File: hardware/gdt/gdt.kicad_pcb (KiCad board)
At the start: 2 copper layers, 76.8 x 34.3 mm, 28 parts, among them J1 USB_OTG, J2 USB_A, Q1 Q_NPN_BEC, Q2 Q_NPN_BEC, Q3 Q_NMOS_GDS, U1 CH340G, U2 AP1117-33, U3 ESP-12E, Y1 12M

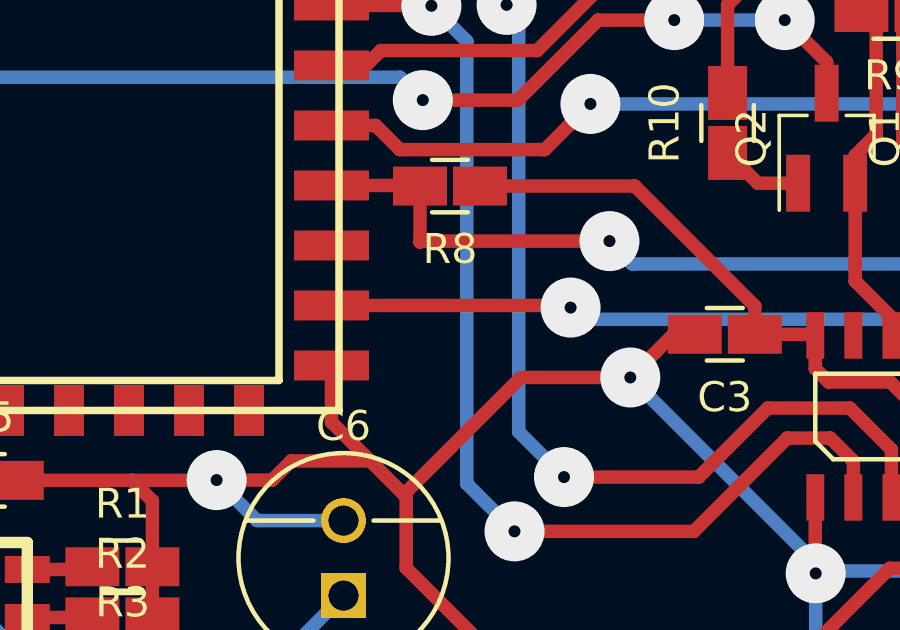
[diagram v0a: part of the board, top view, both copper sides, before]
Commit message: Whoops; this put it into boot mode 5 during reset rather than 1 -- forgot a pulldown resistor.
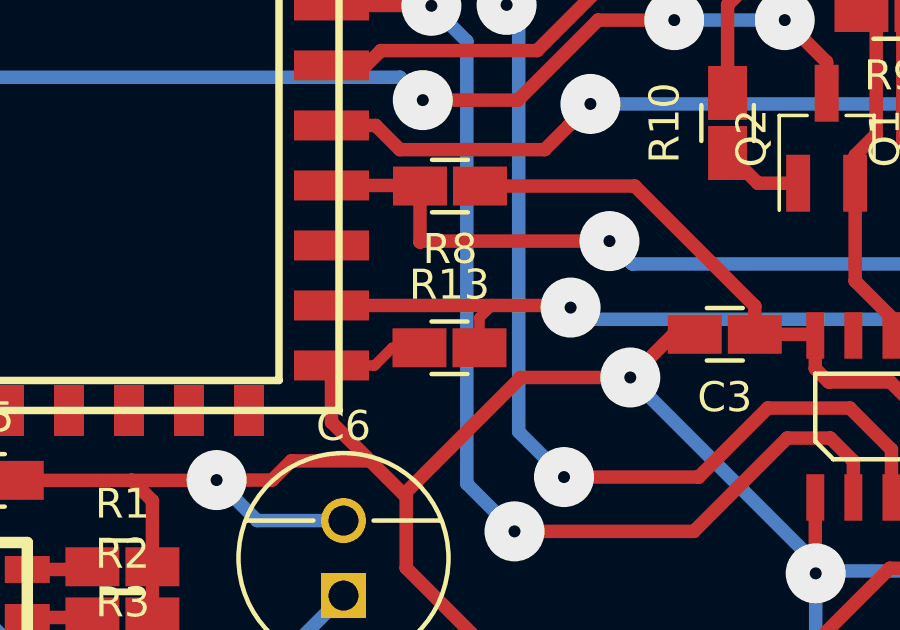
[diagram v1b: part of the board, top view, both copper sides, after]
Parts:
- added R13: 10k, coddingtonbear/coddingtonbear.pretty:0805_Milling, F.Cu at (121.4, 53.3)
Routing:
- net GND: track 186.7 -> 189.9 mm
- net Net-(Q3-Pad1): track 43.1 -> 44.7 mm
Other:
- net class Default: trace_width 0.45 -> 0.25
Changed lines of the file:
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@@
     (thickness 1.6)
     (drawings 4)
-    (tracks 349)
+    (tracks 355)
     (zones 0)
-    (modules 28)
+    (modules 29)
     (nets 42)
   )
@@
   )
   (setup
-    (last_trace_width 0.45)
+    (last_trace_width 0.35)
     (user_trace_width 0.35)
     (trace_clearance 0.2)
@@
   (net_class Default "This is the default net class."
     (clearance 0.2)
-    (trace_width 0.45)
+    (trace_width 0.25)
     (via_dia 2)
     (via_drill 0.4)
@@
     (add_net RXD)
     (add_net TXD)
+  )
+  (module coddingtonbear/coddingtonbear.pretty:0805_Milling (layer F.Cu)
+    (at 121.412 53.34)
+    (descr "Resistor SMD 0805, reflow soldering, Vishay (see dcrcw.pdf)")
+    (tags "resistor 0805")
+    (attr smd)
+    (fp_text reference R13 (at 0 -2.1) (layer F.SilkS)
+      (effects (font (size 1 1) (thickness 0.15)))
+    )
+    (fp_text value 10k (at 0 2.1) (layer F.Fab)
+      (effects (font (size 1 1) (thickness 0.15)))
+    )
+    (fp_line (start -0.6 -0.875) (end 0.6 -0.875) (layer F.SilkS) (width 0.15))
+    (fp_line (start 0.6 0.875) (end -0.6 0.875) (layer F.SilkS) (width 0.15))
+    (pad 2 smd rect (at 1 0) (size 1.8 1.3) (layers F.Cu F.Paste F.Mask)
+      (net 41 "Net-(Q3-Pad1)"))
+    (pad 1 smd rect (at -1 0) (size 1.8 1.3) (layers F.Cu F.Paste F.Mask)
+      (net 2 GND))
+    (model Resistors_SMD.3dshapes/R_0805.wrl
+      (at (xyz 0 0 0))
+      (scale (xyz 1 1 1))
+      (rotate (xyz 0 0 0))
+    )
   )
   (module KiCad/TO_SOT_Packages_SMD.pretty:SOT-23_Handsoldering (layer F.Cu)
@@
   (segment (start 137.415 60.235) (end 137.87 60.69) (width 0.45) (layer F.Cu) (net 1) (status C00000))
   (segment (start 122.7812 67.03) (end 128.979 67.03) (width 0.45) (layer F.Cu) (net 1) (status C00000))
+  (segment (start 120.412 53.34) (end 119.507 53.34) (width 0.35) (layer F.Cu) (net 2) (status 400000))
+  (segment (start 118.917 53.93) (end 117.48 53.93) (width 0.35) (layer F.Cu) (net 2) (status 800000))
+  (segment (start 119.507 53.34) (end 118.917 53.93) (width 0.35) (layer F.Cu) (net 2))
   (via (at 155.105 41.364) (size 2) (drill 0.4) (layers F.Cu B.Cu) (net 2))
   (segment (start 157.385 44.435) (end 157.385 43.644) (width 0.45) (layer F.Cu) (net 2) (status 400000))
@@
   (via (at 158.369 57.023) (size 2) (drill 0.4) (layers F.Cu B.Cu) (net 40))
   (segment (start 156.336 54.99) (end 158.369 57.023) (width 0.45) (layer B.Cu) (net 40))
-  (segment (start 117.48 51.93) (end 125.38 51.93) (width 0.45) (layer F.Cu) (net 41) (status 400000))
+  (segment (start 122.412 53.34) (end 122.412 52.34) (width 0.35) (layer F.Cu) (net 41) (status 400000))
+  (segment (start 122.412 52.34) (end 122.822 51.93) (width 0.35) (layer F.Cu) (net 41))
+  (segment (start 117.48 51.93) (end 122.822 51.93) (width 0.45) (layer F.Cu) (net 41) (status 400000))
+  (segment (start 122.822 51.93) (end 125.38 51.93) (width 0.45) (layer F.Cu) (net 41))
   (segment (start 149.36 60.07) (end 153.2 60.07) (width 0.45) (layer B.Cu) (net 41) (status 800000))
   (segment (start 147.38 58.09) (end 149.36 60.07) (width 0.45) (layer B.Cu) (net 41))

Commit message: Uploading final version of hardware/software.
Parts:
- removed Q3: Q_NMOS_GDS, cpavlina/kicad-pcblib/pth-semi.pretty:TO-220
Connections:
- J2 pad 1: Net-(J2-Pad1) -> +5V
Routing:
- net Net-(R13-Pad2): track 44.7 -> 6.92 mm, vias 3 -> 0
- net Net-(J2-Pad1): track 12.0 -> 0.00 mm, vias 1 -> 0
- net +5V: track 64.3 -> 68.0 mm, vias 1 -> 2
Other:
- net class Default: trace_width 0.25 -> 0.45
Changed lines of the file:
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@@
     (thickness 1.6)
     (drawings 4)
-    (tracks 355)
+    (tracks 337)
     (zones 0)
-    (modules 29)
-    (nets 42)
+    (modules 28)
+    (nets 41)
   )
   (page A4)
@@
   )
   (setup
-    (last_trace_width 0.35)
+    (last_trace_width 0.45)
     (user_trace_width 0.35)
     (trace_clearance 0.2)
@@
   (net 38 LED_G)
   (net 39 LED_R)
-  (net 40 "Net-(J2-Pad1)")
-  (net 41 "Net-(Q3-Pad1)")
+  (net 40 "Net-(R13-Pad2)")
   (net_class Default "This is the default net class."
     (clearance 0.2)
-    (trace_width 0.25)
+    (trace_width 0.45)
     (via_dia 2)
     (via_drill 0.4)
@@
     (add_net "Net-(J1-Pad3)")
     (add_net "Net-(J1-Pad4)")
-    (add_net "Net-(J2-Pad1)")
     (add_net "Net-(J2-Pad2)")
     (add_net "Net-(J2-Pad3)")
     (add_net "Net-(Q1-Pad1)")
     (add_net "Net-(Q2-Pad1)")
-    (add_net "Net-(Q3-Pad1)")
+    (add_net "Net-(R13-Pad2)")
     (add_net "Net-(R5-Pad1)")
     (add_net "Net-(R6-Pad2)")
@@
     (fp_line (start 0.6 0.875) (end -0.6 0.875) (layer F.SilkS) (width 0.15))
     (pad 2 smd rect (at 1 0) (size 1.8 1.3) (layers F.Cu F.Paste F.Mask)
-      (net 41 "Net-(Q3-Pad1)"))
+      (net 40 "Net-(R13-Pad2)"))
     (pad 1 smd rect (at -1 0) (size 1.8 1.3) (layers F.Cu F.Paste F.Mask)
       (net 2 GND))
@@
       (scale (xyz 1 1 1))
       (rotate (xyz 0 0 90))
-    )
-  )
-  (module cpavlina/kicad-pcblib/pth-semi.pretty:TO-220 (layer F.Cu)
-    (at 153.2 57.53 90)
-    (fp_text reference Q3 (at 0 0 90) (layer F.SilkS)
-      (effects (font (size 0.8 0.8) (thickness 0.15)))
-    )
-    (fp_text value Q_NMOS_GDS (at 0 0 90) (layer F.Fab)
-      (effects (font (size 0.8 0.8) (thickness 0.15)))
-    )
-    (fp_line (start -5 -1.75) (end -4.75 -2) (layer F.Fab) (width 0.15))
-    (fp_line (start -4.5 -2) (end -5 -1.5) (layer F.Fab) (width 0.15))
-    (fp_line (start -5 -1.25) (end -4.25 -2) (layer F.Fab) (width 0.15))
-    (fp_line (start -4 -2) (end -5 -1) (layer F.Fab) (width 0.15))
-    (fp_line (start -5 -2) (end 5 -2) (layer F.Fab) (width 0.15))
-    (fp_line (start 5 2.5) (end 5 -2.5) (layer F.Fab) (width 0.15))
-    (fp_line (start 5 -2.5) (end -5 -2.5) (layer F.Fab) (width 0.15))
-    (fp_line (start -5 -2.5) (end -5 2.5) (layer F.Fab) (width 0.15))
-    (fp_line (start -5 2.5) (end 5 2.5) (layer F.Fab) (width 0.15))
-    (fp_line (start 5.5 2.75) (end 5.5 -3.25) (layer F.CrtYd) (width 0.15))
-    (fp_line (start 5.5 -3.25) (end -5.5 -3.25) (layer F.CrtYd) (width 0.15))
-    (fp_line (start -5.5 -3.25) (end -5.5 2.75) (layer F.CrtYd) (width 0.15))
-    (fp_line (start -5.5 2.75) (end 5.5 2.75) (layer F.CrtYd) (width 0.15))
-    (fp_line (start -3.5 1.5) (end -1.5 1.5) (layer F.SilkS) (width 0.15))
-    (fp_line (start -5.0292 -1.1176) (end -4.1656 -1.9812) (layer F.SilkS) (width 0.35))
-    (fp_line (start -4.572 -2.032) (end -5.08 -1.524) (layer F.SilkS) (width 0.35))
-    (fp_line (start -5.08 -2.032) (end 5.08 -2.032) (layer F.SilkS) (width 0.35))
-    (fp_line (start -5.08 -2.54) (end -5.08 2.54) (layer F.SilkS) (width 0.35))
-    (fp_line (start -5.08 2.54) (end 5.08 2.54) (layer F.SilkS) (width 0.35))
-    (fp_line (start 5.08 2.54) (end 5.08 -2.54) (layer F.SilkS) (width 0.35))
-    (fp_line (start 5.08 -2.54) (end -5.08 -2.54) (layer F.SilkS) (width 0.35))
-    (pad 2 thru_hole circle (at 0 0 90) (size 1.99898 1.99898) (drill 1.27) (layers *.Cu *.Mask F.SilkS)
-      (net 3 +5V))
-    (pad 1 thru_hole rect (at -2.54 0 90) (size 1.99898 1.99898) (drill 1.27) (layers *.Cu *.Mask F.SilkS)
-      (net 41 "Net-(Q3-Pad1)"))
-    (pad 3 thru_hole circle (at 2.54 0 90) (size 1.99898 1.99898) (drill 1.27) (layers *.Cu *.Mask F.SilkS)
-      (net 40 "Net-(J2-Pad1)"))
-    (model to/to220_std.wrl
-      (at (xyz 0 0 0))
-      (scale (xyz 1 1 1))
-      (rotate (xyz 0 0 0))
     )
   )
@@
     (fp_line (start -3.55 -1.5) (end 10.55 -1.5) (layer F.SilkS) (width 0.05))
     (pad 1 smd rect (at 0 -2 90) (size 1.5 6) (layers F.Cu F.Paste F.Mask)
-      (net 40 "Net-(J2-Pad1)"))
+      (net 3 +5V))
     (pad 2 smd rect (at 2.5 -2 90) (size 1.5 6) (layers F.Cu F.Paste F.Mask)
       (net 4 "Net-(J2-Pad2)"))
@@
       (net 2 GND))
     (pad 16 smd rect (at 7.75 8.5) (size 2.5 1) (layers F.Cu F.Paste F.Mask)
-      (net 41 "Net-(Q3-Pad1)"))
+      (net 40 "Net-(R13-Pad2)"))
     (pad 17 smd rect (at 7.75 6.5) (size 2.5 1) (layers F.Cu F.Paste F.Mask)
       (net 9 "Net-(U3-Pad17)"))
@@
   (segment (start 137.65 64.67) (end 139.87 62.45) (width 0.45) (layer F.Cu) (net 2) (status 400000))
   (segment (start 139.87 62.45) (end 139.87 60.69) (width 0.45) (layer F.Cu) (net 2) (status 800000))
+  (segment (start 157.54 59.47) (end 157.54 57.337) (width 0.45) (layer B.Cu) (net 3))
+  (segment (start 155.91 71.09) (end 155.87 71.13) (width 0.45) (layer B.Cu) (net 3))
+  (segment (start 155.87 71.13) (end 151.48 71.13) (width 0.45) (layer B.Cu) (net 3))
+  (segment (start 151.48 71.13) (end 150.38 70.03) (width 0.45) (layer B.Cu) (net 3))
+  (segment (start 150.38 70.03) (end 150.38 68.7) (width 0.45) (layer B.Cu) (net 3))
+  (segment (start 150.38 68.7) (end 157.54 61.54) (width 0.45) (layer B.Cu) (net 3))
+  (segment (start 157.54 61.54) (end 157.54 59.47) (width 0.45) (layer B.Cu) (net 3))
   (via (at 155.91 71.09) (size 2) (drill 0.4) (layers F.Cu B.Cu) (net 3))
-  (segment (start 153.2 57.53) (end 155.6 57.53) (width 0.45) (layer B.Cu) (net 3) (status 400000))
-  (segment (start 157.54 59.47) (end 155.6 57.53) (width 0.45) (layer B.Cu) (net 3))
-  (segment (start 157.54 61.54) (end 157.54 59.47) (width 0.45) (layer B.Cu) (net 3))
-  (segment (start 150.38 68.7) (end 157.54 61.54) (width 0.45) (layer B.Cu) (net 3))
-  (segment (start 150.38 70.03) (end 150.38 68.7) (width 0.45) (layer B.Cu) (net 3))
-  (segment (start 151.48 71.13) (end 150.38 70.03) (width 0.45) (layer B.Cu) (net 3))
-  (segment (start 155.87 71.13) (end 151.48 71.13) (width 0.45) (layer B.Cu) (net 3))
-  (segment (start 155.87 71.13) (end 155.91 71.09) (width 0.45) (layer B.Cu) (net 3))
+  (segment (start 157.385 55.34) (end 157.385 51.435) (width 0.45) (layer F.Cu) (net 3) (status 800000))
+  (segment (start 156.464 56.261) (end 157.385 55.34) (width 0.45) (layer F.Cu) (net 3))
+  (via (at 156.464 56.261) (size 2) (drill 0.4) (layers F.Cu B.Cu) (net 3))
+  (segment (start 157.54 57.337) (end 156.464 56.261) (width 0.45) (layer B.Cu) (net 3))
   (segment (start 157.51 69.49) (end 157.51 69.48) (width 0.35) (layer F.Cu) (net 3))
   (segment (start 155.91 71.09) (end 157.51 69.49) (width 0.45) (layer F.Cu) (net 3))
@@
   (segment (start 99.33 50.96) (end 100.36 49.93) (width 0.45) (layer F.Cu) (net 39))
   (segment (start 100.36 49.93) (end 101.98 49.93) (width 0.45) (layer F.Cu) (net 39) (status 800000))
-  (segment (start 153.2 54.99) (end 156.336 54.99) (width 0.45) (layer B.Cu) (net 40) (status 400000))
-  (segment (start 157.385 56.039) (end 157.385 51.435) (width 0.45) (layer F.Cu) (net 40) (status 800000))
-  (segment (start 158.369 57.023) (end 157.385 56.039) (width 0.45) (layer F.Cu) (net 40))
-  (via (at 158.369 57.023) (size 2) (drill 0.4) (layers F.Cu B.Cu) (net 40))
-  (segment (start 156.336 54.99) (end 158.369 57.023) (width 0.45) (layer B.Cu) (net 40))
-  (segment (start 122.412 53.34) (end 122.412 52.34) (width 0.35) (layer F.Cu) (net 41) (status 400000))
-  (segment (start 122.412 52.34) (end 122.822 51.93) (width 0.35) (layer F.Cu) (net 41))
-  (segment (start 117.48 51.93) (end 122.822 51.93) (width 0.45) (layer F.Cu) (net 41) (status 400000))
-  (segment (start 122.822 51.93) (end 125.38 51.93) (width 0.45) (layer F.Cu) (net 41))
-  (segment (start 149.36 60.07) (end 153.2 60.07) (width 0.45) (layer B.Cu) (net 41) (status 800000))
-  (segment (start 147.38 58.09) (end 149.36 60.07) (width 0.45) (layer B.Cu) (net 41))
-  (segment (start 147.38 54.55) (end 147.38 58.09) (width 0.45) (layer B.Cu) (net 41))
-  (segment (start 147.47 54.46) (end 147.38 54.55) (width 0.45) (layer B.Cu) (net 41))
-  (via (at 147.47 54.46) (size 2) (drill 0.4) (layers F.Cu B.Cu) (net 41))
-  (segment (start 147.42 54.46) (end 147.47 54.46) (width 0.45) (layer F.Cu) (net 41))
-  (segment (start 143.95 50.99) (end 147.42 54.46) (width 0.45) (layer F.Cu) (net 41))
-  (segment (start 142.94 50.99) (end 143.95 50.99) (width 0.45) (layer F.Cu) (net 41))
-  (segment (start 142.24 50.29) (end 142.94 50.99) (width 0.45) (layer F.Cu) (net 41))
-  (via (at 142.24 50.29) (size 2) (drill 0.4) (layers F.Cu B.Cu) (net 41))
-  (segment (start 140.14 52.39) (end 142.24 50.29) (width 0.45) (layer B.Cu) (net 41))
-  (segment (start 125.84 52.39) (end 140.14 52.39) (width 0.45) (layer B.Cu) (net 41))
-  (segment (start 125.45 52) (end 125.84 52.39) (width 0.45) (layer B.Cu) (net 41))
-  (via (at 125.45 52) (size 2) (drill 0.4) (layers F.Cu B.Cu) (net 41))
-  (segment (start 125.38 51.93) (end 125.45 52) (width 0.45) (layer F.Cu) (net 41))
+  (segment (start 122.412 53.34) (end 122.412 52.34) (width 0.35) (layer F.Cu) (net 40) (status 400000))
+  (segment (start 122.412 52.34) (end 122.822 51.93) (width 0.35) (layer F.Cu) (net 40))
+  (segment (start 117.48 51.93) (end 122.822 51.93) (width 0.45) (layer F.Cu) (net 40) (status 400000))
 )
